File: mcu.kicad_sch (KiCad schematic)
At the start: 0 parts

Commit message: Draw power schematic.
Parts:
- added C10: 22uF, Capacitor_SMD:C_0603_1608Metric_Pad1.08x0.95mm_HandSolder, symbol Device:C
- added C11, C9: 100nF, Capacitor_SMD:C_0603_1608Metric_Pad1.08x0.95mm_HandSolder, symbol Device:C
- added Q4, Q5: SS8050, Package_TO_SOT_SMD:SOT-23, symbol Transistor_BJT:SS8050
- added R14, R15, R16, R17, R18, R19, R20: 10K, Resistor_SMD:R_0603_1608Metric_Pad0.98x0.95mm_HandSolder, symbol Device:R
- added U2: ESP32-WROOM-32D, RF_Module:ESP32-WROOM-32D, symbol RF_Module:ESP32-WROOM-32D
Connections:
- new net: Q5.1 (B), R20.1
- new net: Q4.1 (B), R19.1
- new net: C11.1, Q4.3 (C), R14.1, U2.3 (EN)
- new net BATT_I2C.SCL: R17.1
- new net BATT_I2C.SDA: R16.1
- new net Disp.SCL: R18.1
- new net Disp.SDA: R15.1
- new net GNDD: C10.2, C11.2, C9.2, U2.1 (GND), U2.15 (GND), U2.38 (GND), U2.39 (GND)
- new net IO0: Q5.3 (C), U2.25 (IO0)
- new net MCU.DTR: Q5.2 (E), R19.2
- new net MCU.RTS: Q4.2 (E), R20.2
- new net MCU.RX: U2.34 (RXD0/IO3)
- new net MCU.TX: U2.35 (TXD0/IO1)
- new net VDD: C10.1, C9.1, R14.2, R15.2, R16.2, R17.2, R18.2, U2.2 (VDD)
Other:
- note added: "Transistor MPN check!"

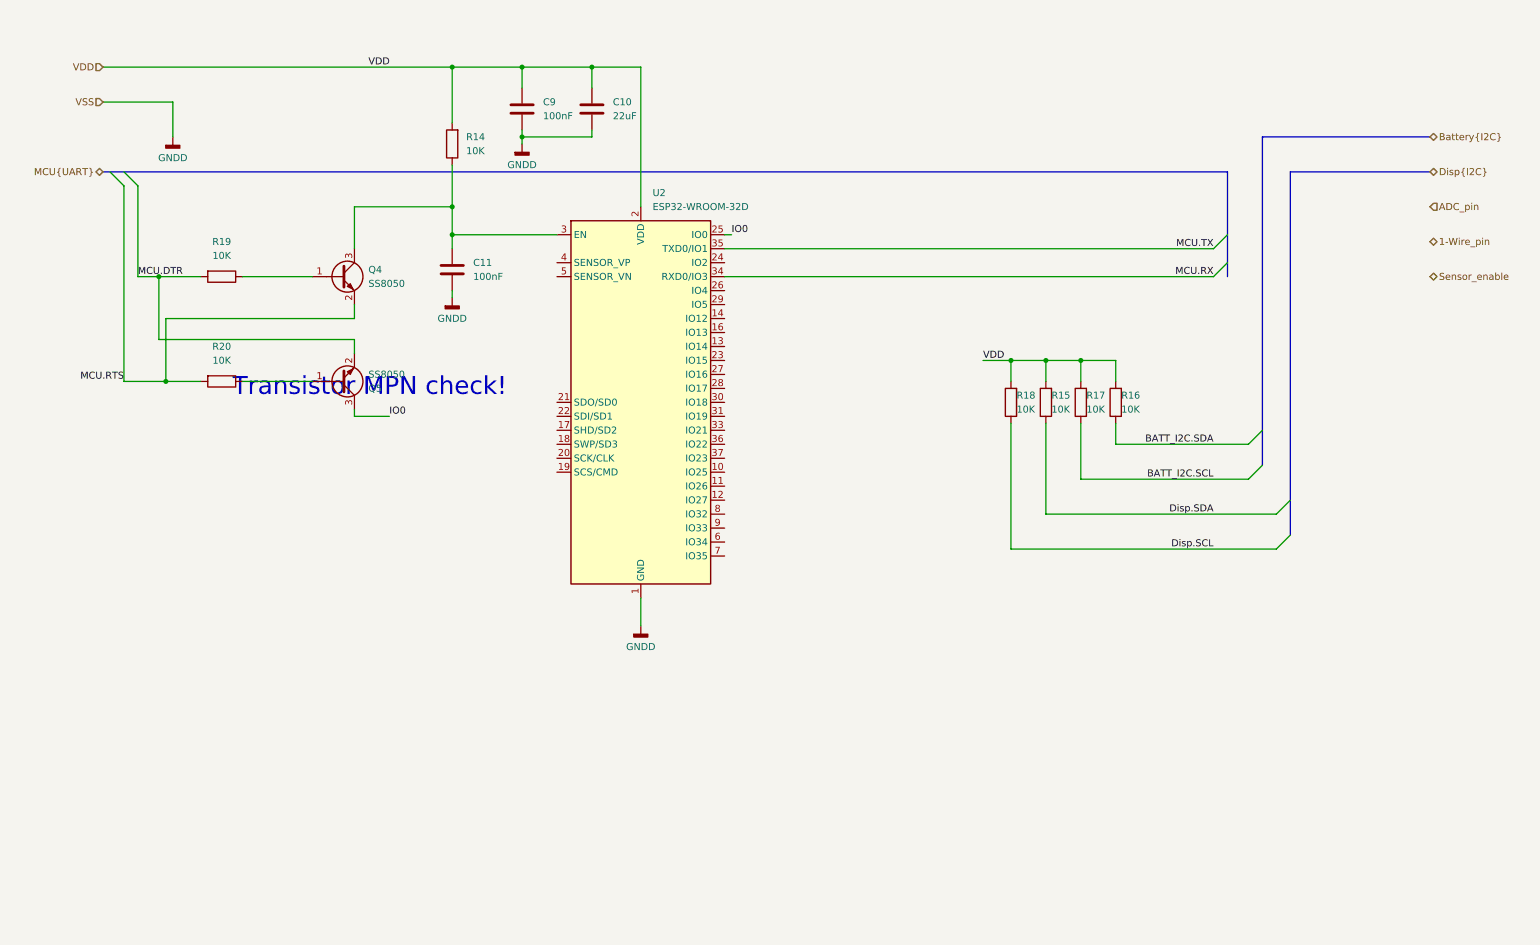
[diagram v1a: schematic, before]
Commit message: Change BJT to FET in MCU. Add pinout.
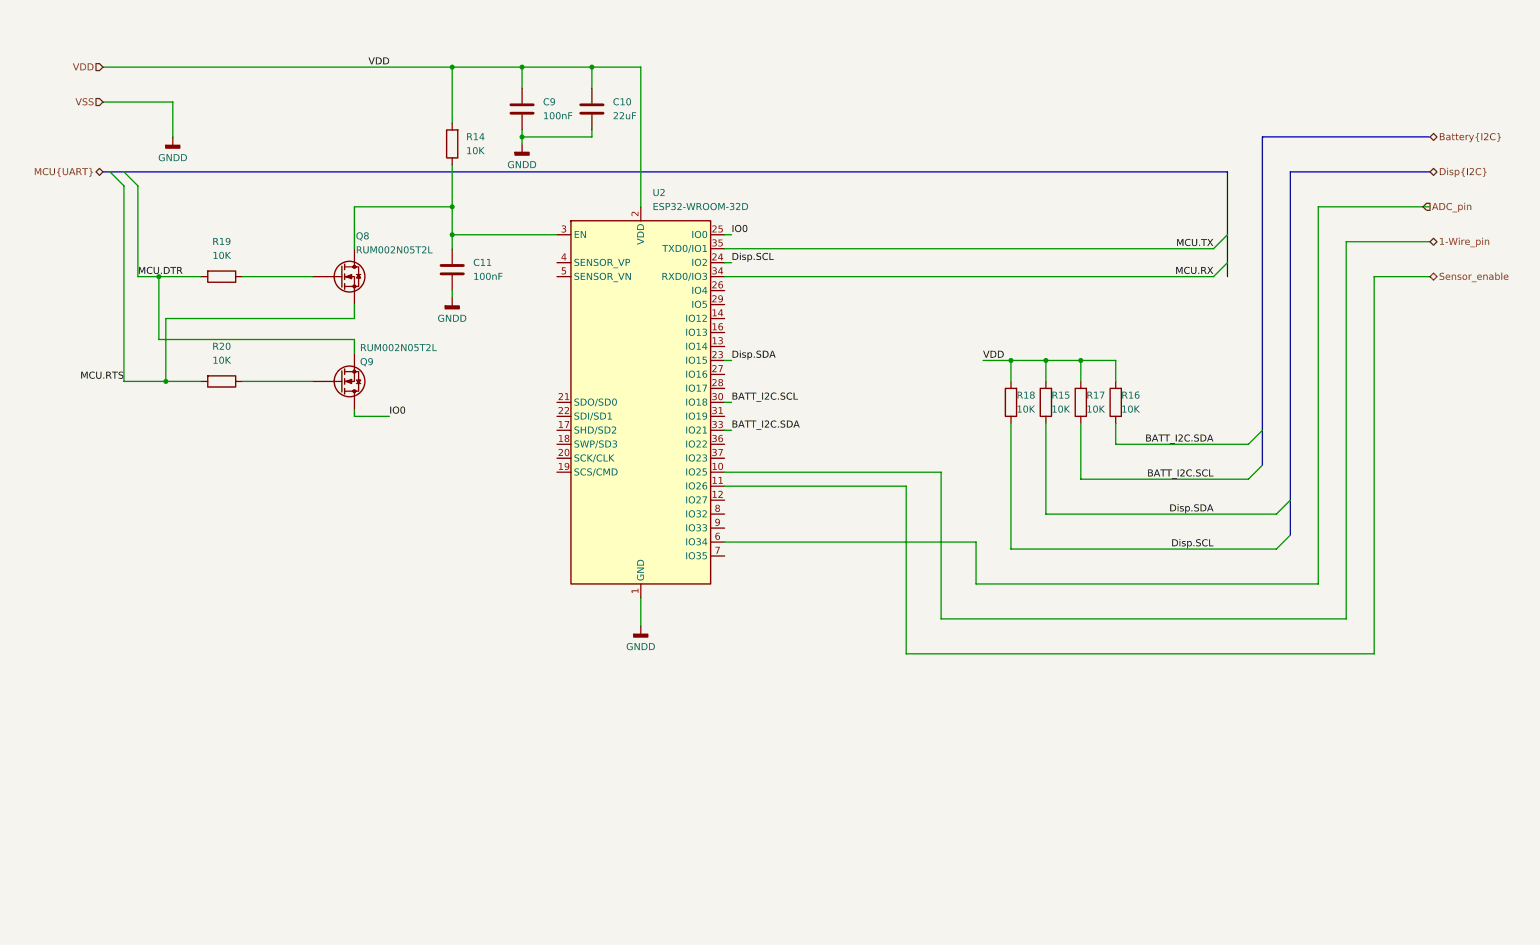
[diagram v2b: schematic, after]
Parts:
- removed Q4, Q5: SS8050, Package_TO_SOT_SMD:SOT-23, symbol Transistor_BJT:SS8050
- added Q8, Q9: RUM002N05T2L, Package_TO_SOT_SMD:SOT-723, symbol Device:Q_NMOS
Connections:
- net 1-Wire_pin: now also U2.10 (IO25)
- net ADC_pin: now also U2.6 (IO34)
- net BATT_I2C.SCL: now also U2.30 (IO18)
- net BATT_I2C.SDA: now also U2.33 (IO21)
- net Disp.SCL: now also U2.24 (IO2)
- net Disp.SDA: now also U2.23 (IO15)
- net IO0: now also Q9.3 (D)
- net MCU.DTR: now also Q9.2 (S)
- net MCU.RTS: now also Q8.2 (S)
- net Sensor_enable: now also U2.11 (IO26)
- net at R20.1: now also Q9.1 (G)
- net at R19.1: now also Q8.1 (G)
- net at C11.1, R14.1, U2.3 (EN): now also Q8.3 (D)
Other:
- note removed: "Transistor MPN check!"

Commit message: Add analog schematic and refine wiring on top.
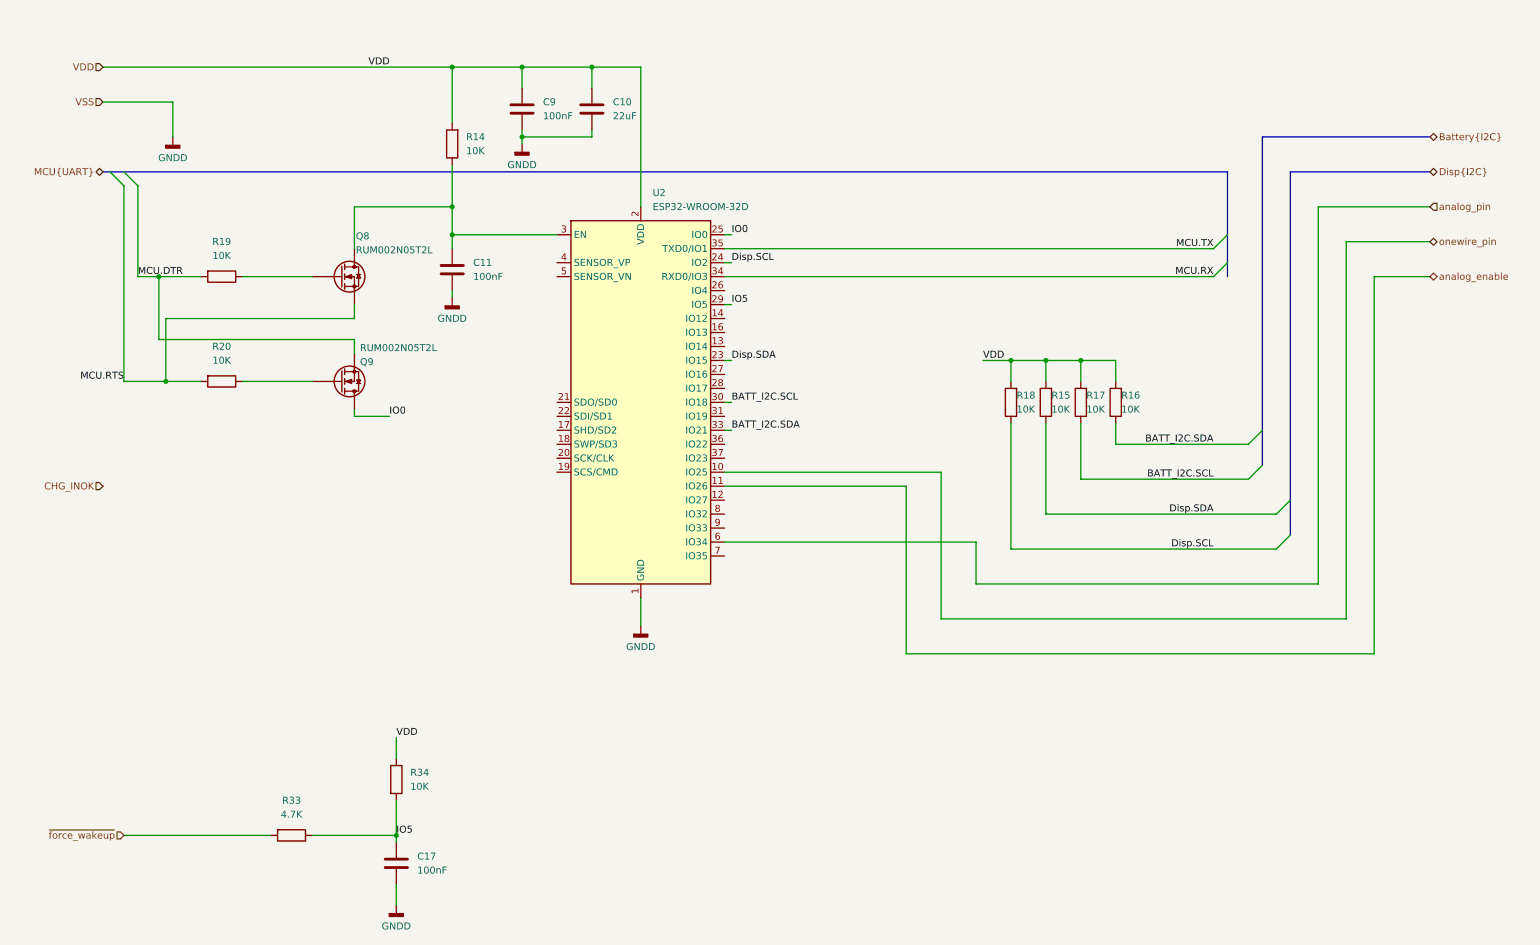
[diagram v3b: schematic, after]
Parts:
- added C17: 100nF, Capacitor_SMD:C_0603_1608Metric_Pad1.08x0.95mm_HandSolder, symbol Device:C
- added R33: 4.7K, Resistor_SMD:R_0603_1608Metric_Pad0.98x0.95mm_HandSolder, symbol Device:R
- added R34: 10K, Resistor_SMD:R_0603_1608Metric_Pad0.98x0.95mm_HandSolder, symbol Device:R
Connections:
- net GNDD: now also C17.2
- net VDD: now also R34.1
- net IO5: now reaches U2.29 (IO5)
- net IO5: now also C17.1, R33.1, R34.2
- net 1-Wire_pin renamed onewire_pin
- net ADC_pin renamed analog_pin
- net Sensor_enable renamed analog_enable
- new net ~{force_wakeup}: R33.2

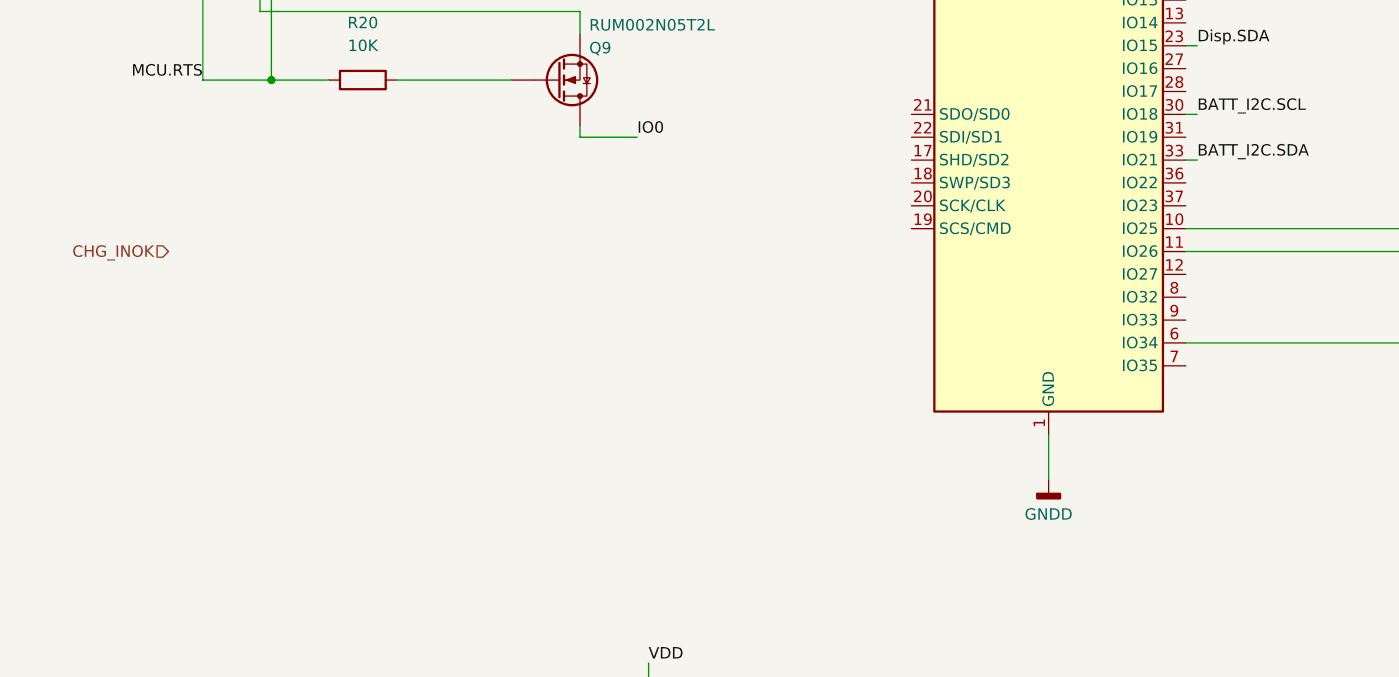
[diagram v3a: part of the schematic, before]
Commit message: Add charger, battery cell.
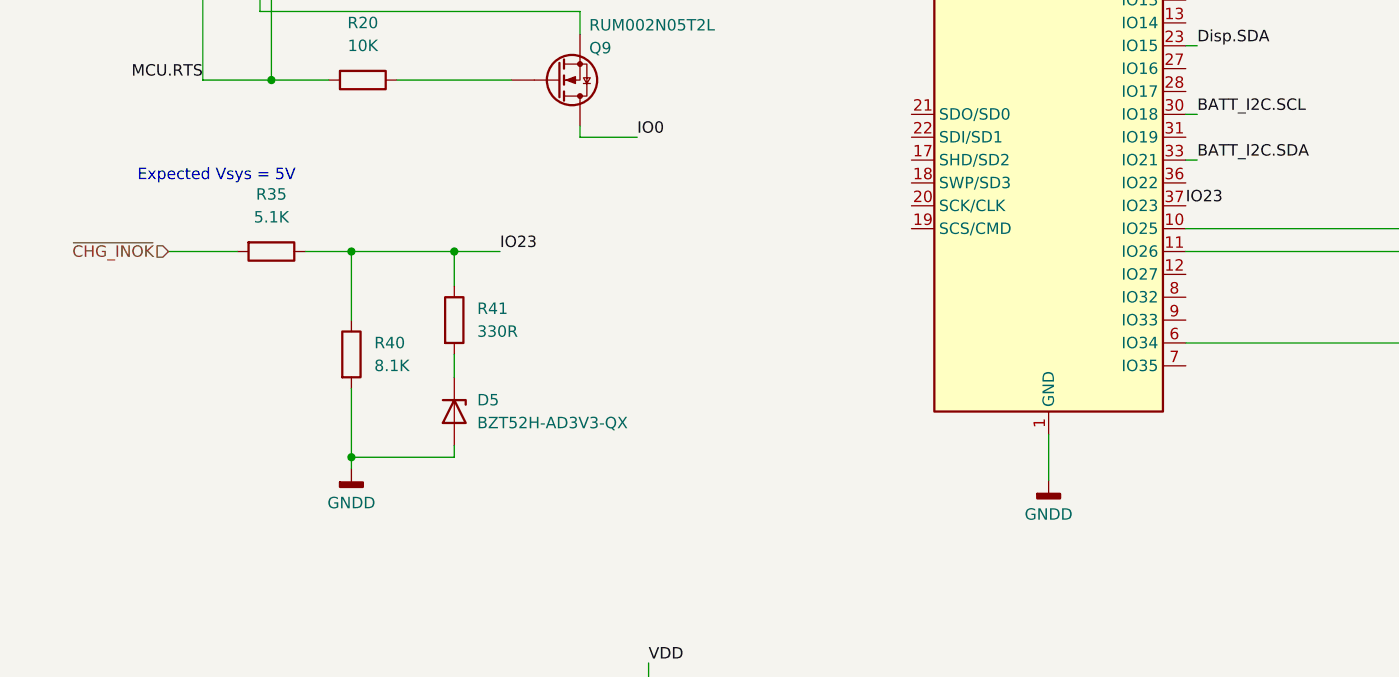
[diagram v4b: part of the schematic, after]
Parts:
- added D5: BZT52H-AD3V3-QX, Diode_SMD:D_SOD-123F, symbol Diode:BZT52Bxx
- added R35: 5.1K, Resistor_SMD:R_0603_1608Metric_Pad0.98x0.95mm_HandSolder, symbol Device:R
- added R40: 8.1K, Resistor_SMD:R_0603_1608Metric_Pad0.98x0.95mm_HandSolder, symbol Device:R
- added R41: 330R, Resistor_SMD:R_0603_1608Metric_Pad0.98x0.95mm_HandSolder, symbol Device:R
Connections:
- net GNDD: now also D5.2 (A), R40.2
- net IO23: now reaches U2.37 (IO23)
- net IO23: now also R35.1, R40.1, R41.1
- new net: D5.1 (K), R41.2
- new net ~{CHG_INOK}: R35.2
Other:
- note added: "Expected Vsys = 5V"

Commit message: Fix issues
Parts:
- D5, R35, R40, R41: now not fitted
- R33: value 4.7K -> 100R
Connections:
- net IO0 renamed BOOT
- net IO23 renamed ~{CHG_INOK_PROT}
- net ~{CHG_INOK_PROT}: now also U2.29 (IO5); no longer U2.37 (IO23)
- net IO5 renamed ~{force_wakeup_prot}
- net ~{force_wakeup_prot}: now also U2.37 (IO23); no longer U2.29 (IO5)
